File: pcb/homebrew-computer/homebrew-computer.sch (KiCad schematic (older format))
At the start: 2 parts

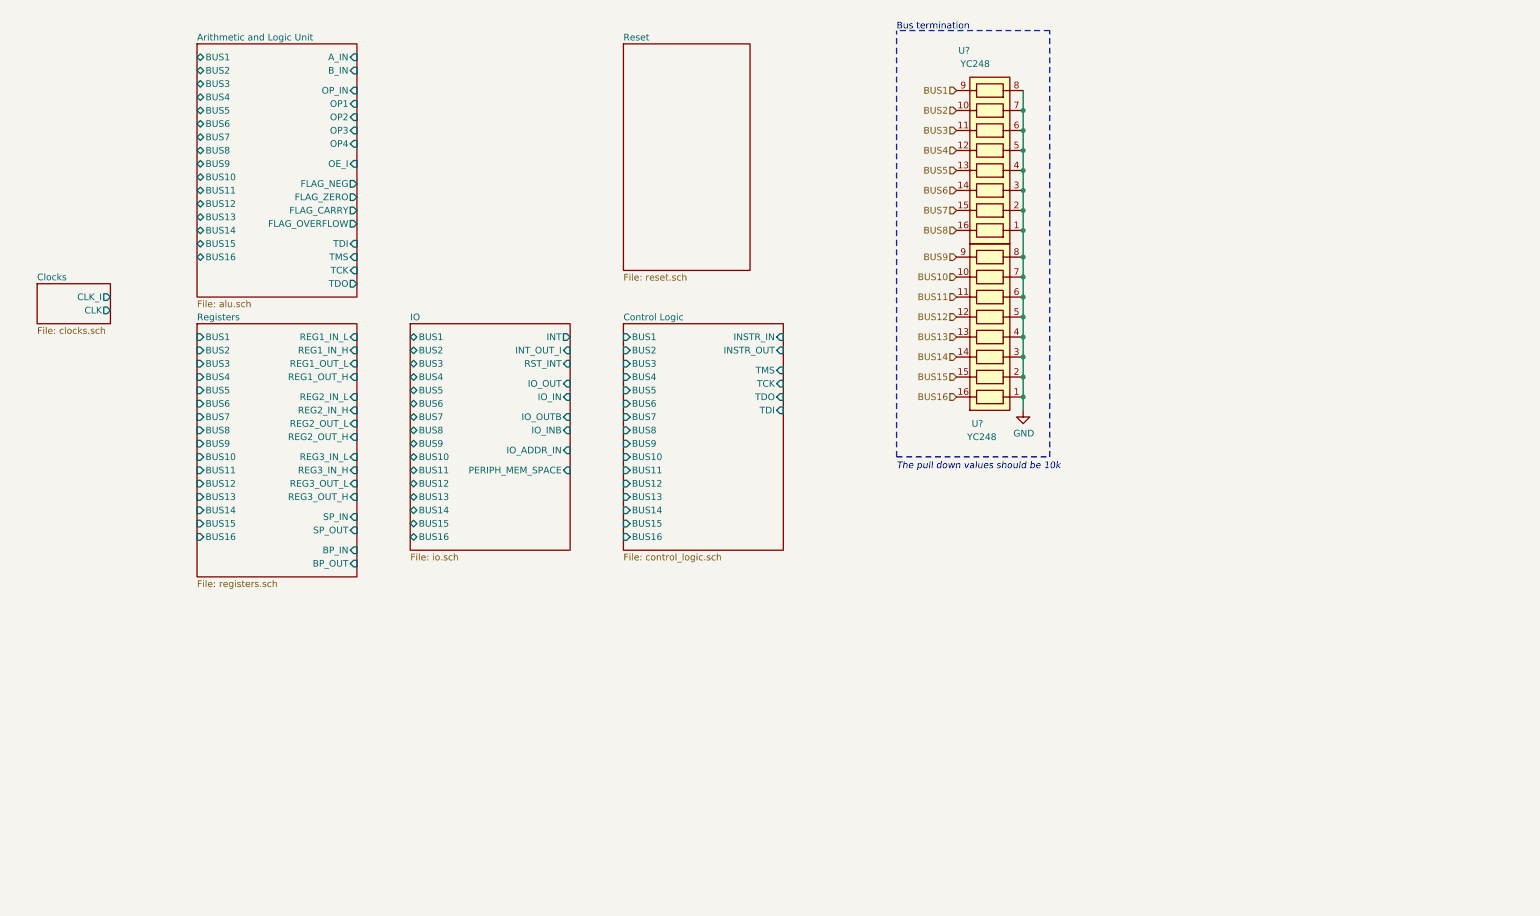
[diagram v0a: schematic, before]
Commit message: Add program counter
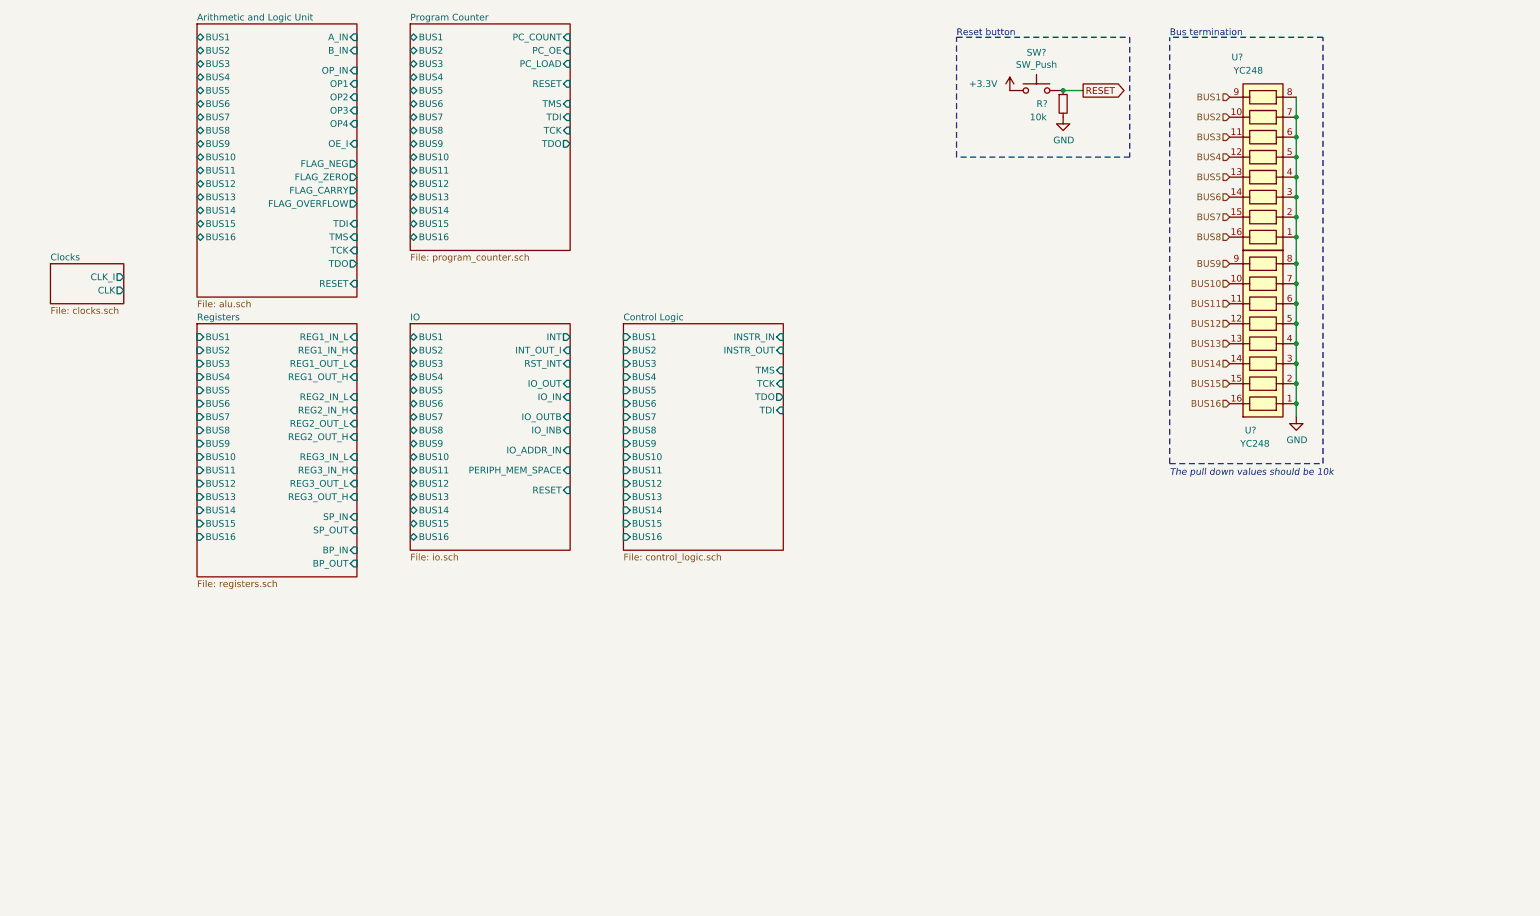
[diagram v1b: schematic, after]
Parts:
- added R?: 10k, symbol Device:R_Small
- added SW?: SW_Push, symbol Switch:SW_Push
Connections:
- net GND: now also R?.2
- new net +3V3: SW?.1
- new net RESET: R?.1, SW?.2
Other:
- note added: "Reset button"
- moved on the sheet: U?

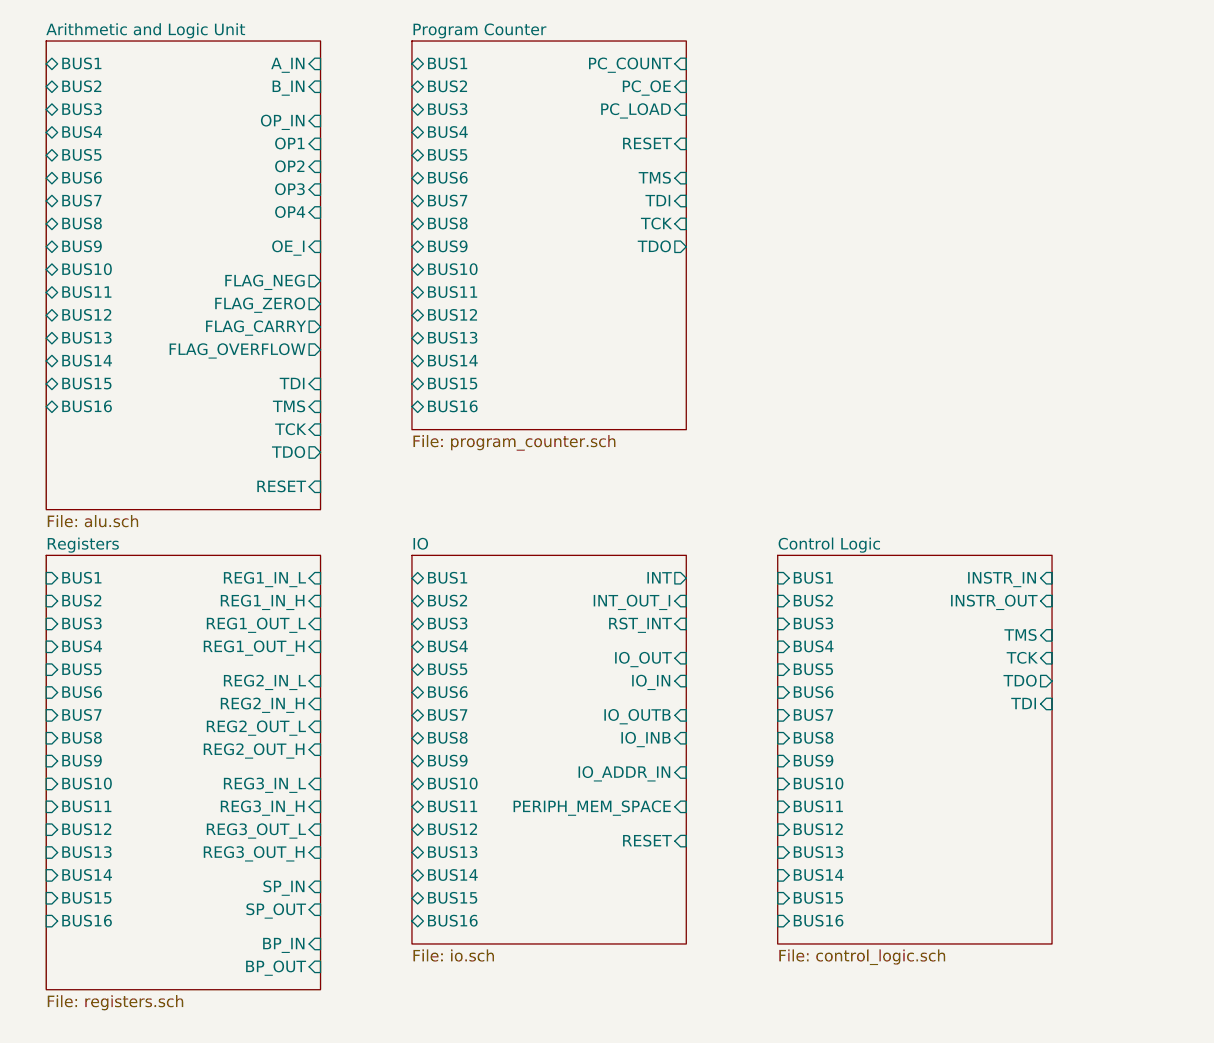
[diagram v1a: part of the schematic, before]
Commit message: Change the control logic CPLD for a bigger one
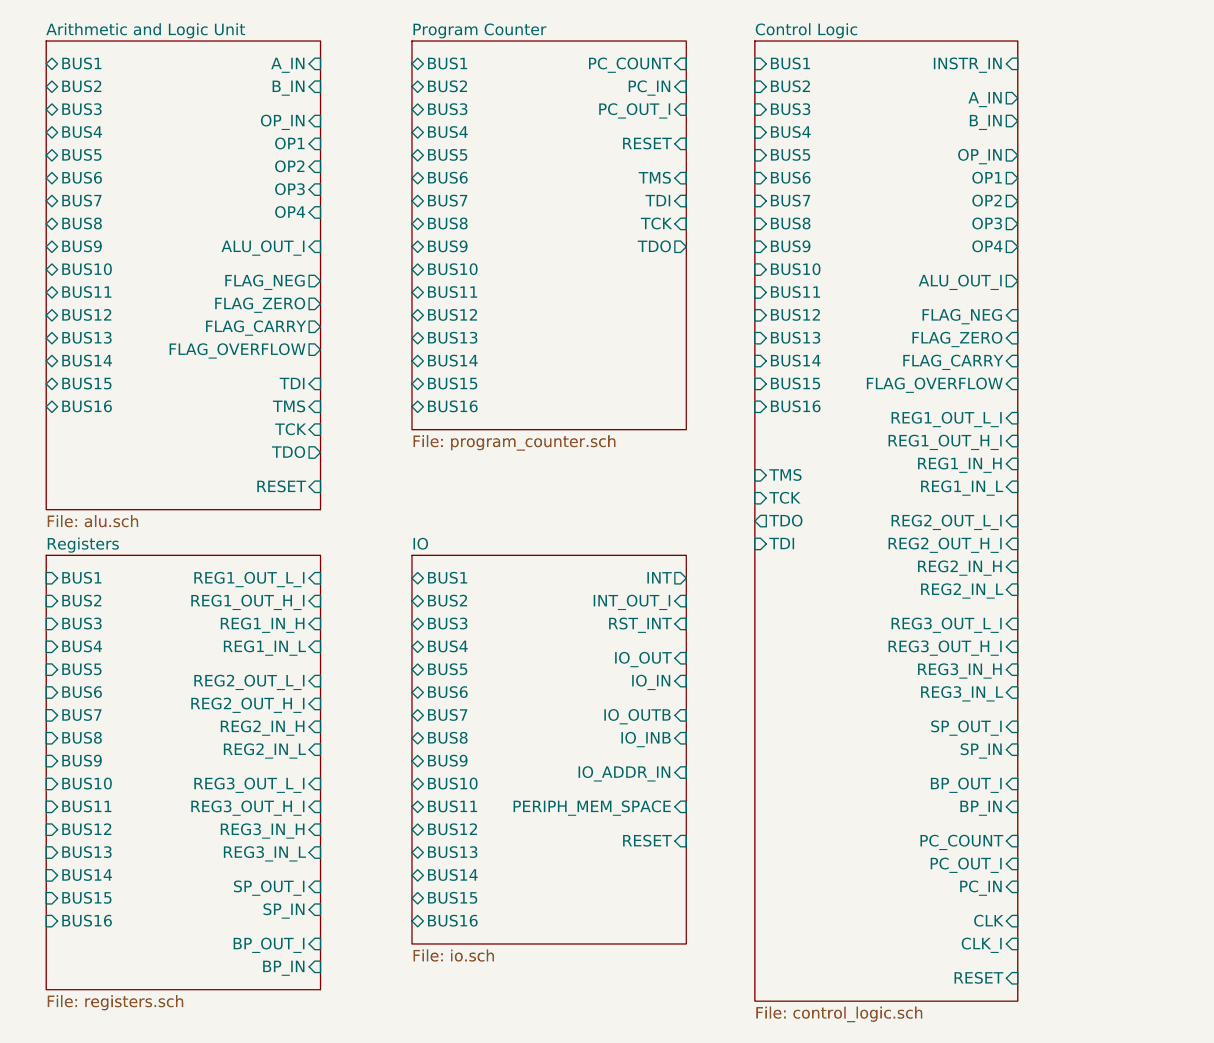
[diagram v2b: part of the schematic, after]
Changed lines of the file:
@@
 F12 "FLAG_CARRY" O R 3450 2100 50
 F13 "FLAG_OVERFLOW" O R 3450 2200 50
-F14 "OE_I" I R 3450 1750 50
+F14 "ALU_OUT_I" I R 3450 1750 50
 F15 "BUS1" T L 2250 950 50
 F16 "BUS2" T L 2250 1050 50
@@
 F33 "OP_IN" I R 3450 1200 50
 F34 "RESET" I R 3450 2800 50
-$EndSheet
-$Sheet
-S 2250 3100 1200 1900
-U 5F8C07F0
-F0 "Registers" 50
-F1 "registers.sch" 50
-F2 "REG1_IN_L" I R 3450 3200 50
-F3 "REG1_IN_H" I R 3450 3300 50
-F4 "REG1_OUT_L" I R 3450 3400 50
-F5 "REG1_OUT_H" I R 3450 3500 50
-F6 "REG2_IN_L" I R 3450 3650 50
-F7 "REG2_IN_H" I R 3450 3750 50
-F8 "REG2_OUT_L" I R 3450 3850 50
-F9 "REG2_OUT_H" I R 3450 3950 50
-F10 "REG3_IN_L" I R 3450 4100 50
-F11 "REG3_IN_H" I R 3450 4200 50
-F12 "REG3_OUT_L" I R 3450 4300 50
-F13 "REG3_OUT_H" I R 3450 4400 50
-F14 "SP_IN" I R 3450 4550 50
-F15 "SP_OUT" I R 3450 4650 50
-F16 "BUS1" I L 2250 3200 50
-F17 "BUS2" I L 2250 3300 50
-F18 "BUS3" I L 2250 3400 50
-F19 "BUS4" I L 2250 3500 50
-F20 "BUS5" I L 2250 3600 50
-F21 "BUS6" I L 2250 3700 50
-F22 "BUS7" I L 2250 3800 50
-F23 "BUS8" I L 2250 3900 50
-F24 "BUS9" I L 2250 4000 50
-F25 "BUS10" I L 2250 4100 50
-F26 "BUS11" I L 2250 4200 50
-F27 "BUS12" I L 2250 4300 50
-F28 "BUS13" I L 2250 4400 50
-F29 "BUS14" I L 2250 4500 50
-F30 "BUS15" I L 2250 4600 50
-F31 "BUS16" I L 2250 4700 50
-F32 "BP_OUT" I R 3450 4900 50
-F33 "BP_IN" I R 3450 4800 50
-$EndSheet
-$Sheet
-S 5450 3100 1200 1700
-U 5F8B5E3D
-F0 "Control Logic" 50
-F1 "control_logic.sch" 50
-F2 "TMS" I R 6650 3450 50
-F3 "TCK" I R 6650 3550 50
-F4 "TDI" I R 6650 3750 50
-F5 "INSTR_IN" I R 6650 3200 50
-F6 "INSTR_OUT" I R 6650 3300 50
-F7 "BUS1" I L 5450 3200 50
-F8 "BUS2" I L 5450 3300 50
-F9 "BUS3" I L 5450 3400 50
-F10 "BUS4" I L 5450 3500 50
-F11 "BUS5" I L 5450 3600 50
-F12 "BUS6" I L 5450 3700 50
-F13 "BUS7" I L 5450 3800 50
-F14 "BUS8" I L 5450 3900 50
-F15 "BUS9" I L 5450 4000 50
-F16 "BUS10" I L 5450 4100 50
-F17 "BUS11" I L 5450 4200 50
-F18 "BUS12" I L 5450 4300 50
-F19 "BUS13" I L 5450 4400 50
-F20 "BUS14" I L 5450 4500 50
-F21 "BUS15" I L 5450 4600 50
-F22 "BUS16" I L 5450 4700 50
-F23 "TDO" O R 6650 3650 50
 $EndSheet
 $Sheet
@@
 F20 "BUS16" T L 3850 2450 50
 F21 "PC_COUNT" I R 5050 950 50
-F22 "PC_OE" I R 5050 1050 50
-F23 "RESET" I R 5050 1300 50
-F24 "PC_LOAD" I R 5050 1150 50
-F25 "TDO" O R 5050 1750 50
+F22 "RESET" I R 5050 1300 50
+F23 "TDO" O R 5050 1750 50
+F24 "PC_IN" I R 5050 1050 50
+F25 "PC_OUT_I" I R 5050 1150 50
 $EndSheet
 $Comp
@@
 Text Notes 7950 950  0    50   ~ 0
 Reset button
+$Sheet
+S 2250 3100 1200 1900
+U 5F8C07F0
+F0 "Registers" 50
+F1 "registers.sch" 50
+F2 "BUS1" I L 2250 3200 50
+F3 "BUS2" I L 2250 3300 50
+F4 "BUS3" I L 2250 3400 50
+F5 "BUS4" I L 2250 3500 50
+F6 "BUS5" I L 2250 3600 50
+F7 "BUS6" I L 2250 3700 50
+F8 "BUS7" I L 2250 3800 50
+F9 "BUS8" I L 2250 3900 50
+F10 "BUS9" I L 2250 4000 50
+F11 "BUS10" I L 2250 4100 50
+F12 "BUS11" I L 2250 4200 50
+F13 "BUS12" I L 2250 4300 50
+F14 "BUS13" I L 2250 4400 50
+F15 "BUS14" I L 2250 4500 50
+F16 "BUS15" I L 2250 4600 50
+F17 "BUS16" I L 2250 4700 50
+F18 "REG2_OUT_L_I" I R 3450 3650 50
+F19 "REG2_OUT_H_I" I R 3450 3750 50
+F20 "REG3_OUT_L_I" I R 3450 4100 50
+F21 "REG3_OUT_H_I" I R 3450 4200 50
+F22 "SP_OUT_I" I R 3450 4550 50
+F23 "SP_IN" I R 3450 4650 50
+F24 "BP_OUT_I" I R 3450 4800 50
+F25 "BP_IN" I R 3450 4900 50
+F26 "REG3_IN_H" I R 3450 4300 50
+F27 "REG3_IN_L" I R 3450 4400 50
+F28 "REG1_IN_H" I R 3450 3400 50
+F29 "REG1_IN_L" I R 3450 3500 50
+F30 "REG2_IN_H" I R 3450 3850 50
+F31 "REG2_IN_L" I R 3450 3950 50
+F32 "REG1_OUT_L_I" I R 3450 3200 50
+F33 "REG1_OUT_H_I" I R 3450 3300 50
+$EndSheet
+$Sheet
+S 5350 850  1150 4200
+U 5F8B5E3D
+F0 "Control Logic" 50
+F1 "control_logic.sch" 50
+F2 "TMS" I L 5350 2750 50
+F3 "TCK" I L 5350 2850 50
+F4 "TDI" I L 5350 3050 50
+F5 "BUS1" I L 5350 950 50
+F6 "BUS2" I L 5350 1050 50
+F7 "BUS3" I L 5350 1150 50
+F8 "BUS4" I L 5350 1250 50
+F9 "BUS5" I L 5350 1350 50
+F10 "BUS6" I L 5350 1450 50
+F11 "BUS7" I L 5350 1550 50
+F12 "BUS8" I L 5350 1650 50
+F13 "BUS9" I L 5350 1750 50
+F14 "BUS10" I L 5350 1850 50
+F15 "BUS11" I L 5350 1950 50
+F16 "BUS12" I L 5350 2050 50
+F17 "BUS13" I L 5350 2150 50
+F18 "BUS14" I L 5350 2250 50
+F19 "BUS15" I L 5350 2350 50
+F20 "BUS16" I L 5350 2450 50
+F21 "TDO" O L 5350 2950 50
+F22 "INSTR_IN" I R 6500 950 50
+F23 "A_IN" O R 6500 1100 50
+F24 "B_IN" O R 6500 1200 50
+F25 "OP_IN" O R 6500 1350 50
+F26 "OP1" O R 6500 1450 50
+F27 "OP2" O R 6500 1550 50
+F28 "OP3" O R 6500 1650 50
+F29 "OP4" O R 6500 1750 50
+F30 "ALU_OUT_I" O R 6500 1900 50
+F31 "FLAG_NEG" I R 6500 2050 50
+F32 "FLAG_ZERO" I R 6500 2150 50
+F33 "FLAG_CARRY" I R 6500 2250 50
+F34 "FLAG_OVERFLOW" I R 6500 2350 50
+F35 "REG1_OUT_L_I" I R 6500 2500 50
+F36 "REG1_OUT_H_I" I R 6500 2600 50
+F37 "REG1_IN_H" I R 6500 2700 50
+F38 "REG1_IN_L" I R 6500 2800 50
+F39 "REG2_OUT_L_I" I R 6500 2950 50
+F40 "REG2_OUT_H_I" I R 6500 3050 50
+F41 "REG2_IN_H" I R 6500 3150 50
+F42 "REG2_IN_L" I R 6500 3250 50
+F43 "REG3_OUT_L_I" I R 6500 3400 50
+F44 "REG3_OUT_H_I" I R 6500 3500 50
+F45 "REG3_IN_H" I R 6500 3600 50
+F46 "REG3_IN_L" I R 6500 3700 50
+F47 "SP_OUT_I" I R 6500 3850 50
+F48 "SP_IN" I R 6500 3950 50
+F49 "BP_OUT_I" I R 6500 4100 50
+F50 "BP_IN" I R 6500 4200 50
+F51 "PC_COUNT" I R 6500 4350 50
+F52 "PC_OUT_I" I R 6500 4450 50
+F53 "PC_IN" I R 6500 4550 50
+F54 "CLK" I R 6500 4700 50
+F55 "CLK_I" I R 6500 4800 50
+F56 "RESET" I R 6500 4950 50
+$EndSheet
 $EndSCHEMATC
